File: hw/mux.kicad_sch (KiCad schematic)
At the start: 4 parts, among them U11 NCP708, U6 TS3USB3031

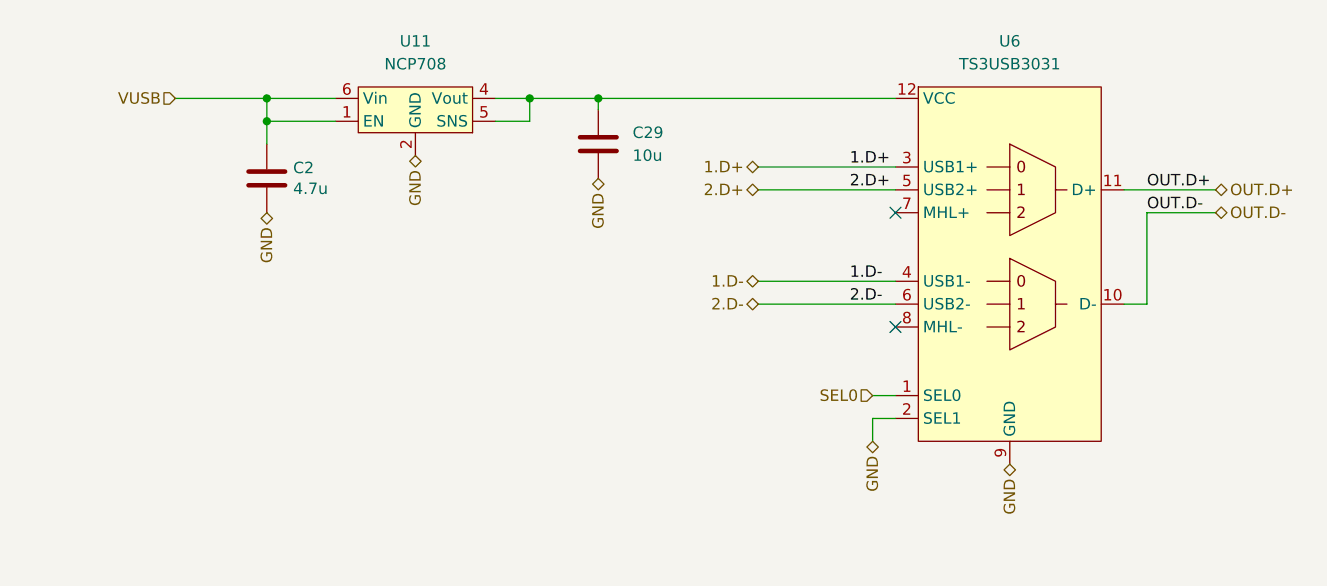
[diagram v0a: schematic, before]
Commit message: Solved issue "Invert INOKB->USB Mux logic"
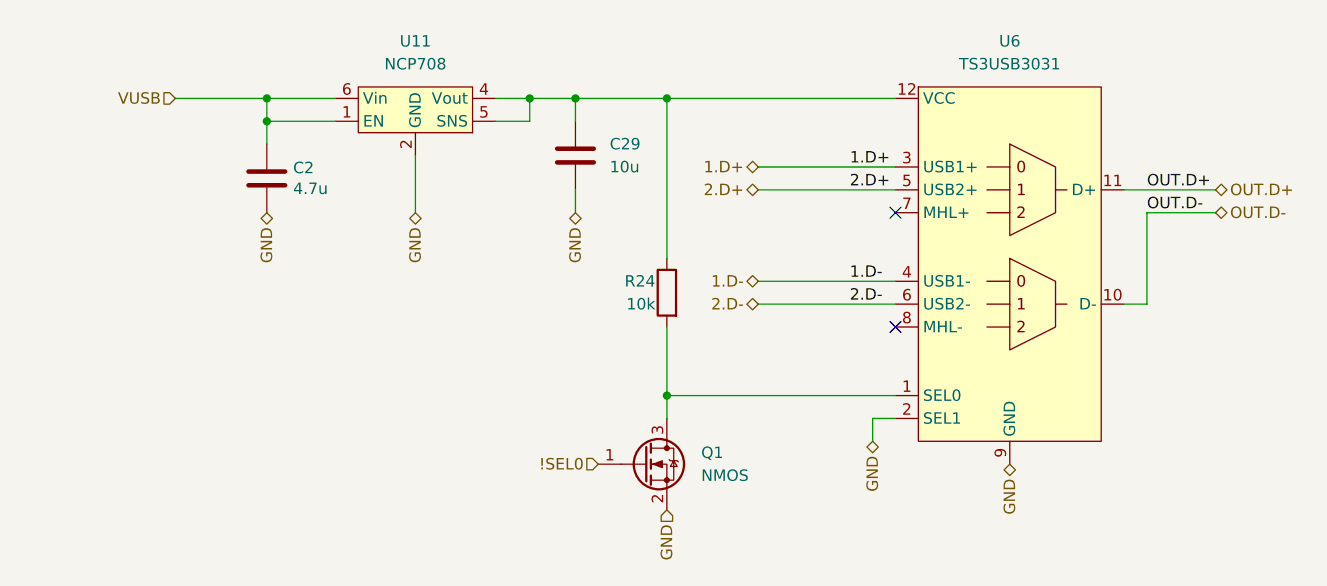
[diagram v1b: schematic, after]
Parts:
- added Q1: NMOS, Package_TO_SOT_SMD:SOT-723, symbol Device:Q_NMOS_GSD
- added R24: 10k, Resistor_SMD:R_0402_1005Metric, symbol Device:R
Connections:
- net GND: now also Q1.2 (S)
- net at C29.1, U11.4 (Vout), U11.5 (SNS)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: now also R24.1
- net SEL0: no longer names the net of U6.1 (SEL0)
- net SEL0: now also Q1.3 (D), R24.2
- new net !SEL0: Q1.1 (G)
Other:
- moved on the sheet: C29
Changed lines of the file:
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@@
   (junction (at 110.49 63.5) (diameter 0) (color 0 0 0 0)
   )
+  (junction (at 144.78 63.5) (diameter 0) (color 0 0 0 0)
+  )
   (junction (at 139.7 63.5) (diameter 0) (color 0 0 0 0)
   )
+  (junction (at 154.94 96.52) (diameter 0) (color 0 0 0 0)
+  )
   (junction (at 110.49 66.04) (diameter 0) (color 0 0 0 0)
   )
-  (junction (at 147.32 63.5) (diameter 0) (color 0 0 0 0)
+  (junction (at 154.94 63.5) (diameter 0) (color 0 0 0 0)
   )
   (no_connect (at 180.34 76.2))
@@
     (stroke (width 0) (type default))
   )
+  (wire (pts (xy 154.94 63.5) (xy 180.34 63.5))
+    (stroke (width 0) (type default))
+  )
   (wire (pts (xy 139.7 66.04) (xy 139.7 63.5))
     (stroke (width 0) (type default))
@@
     (stroke (width 0) (type default))
   )
-  (wire (pts (xy 147.32 63.5) (xy 147.32 64.77))
+  (wire (pts (xy 154.94 88.9) (xy 154.94 96.52))
+    (stroke (width 0) (type default))
+  )
+  (wire (pts (xy 144.78 63.5) (xy 144.78 66.04))
     (stroke (width 0) (type default))
   )
@@
     (stroke (width 0) (type default))
   )
-  (wire (pts (xy 139.7 63.5) (xy 147.32 63.5))
+  (wire (pts (xy 139.7 63.5) (xy 144.78 63.5))
+    (stroke (width 0) (type default))
+  )
+  (wire (pts (xy 154.94 99.06) (xy 154.94 96.52))
+    (stroke (width 0) (type default))
+  )
+  (wire (pts (xy 144.78 63.5) (xy 154.94 63.5))
+    (stroke (width 0) (type default))
+  )
+  (wire (pts (xy 154.94 63.5) (xy 154.94 81.28))
     (stroke (width 0) (type default))
   )
@@
     (stroke (width 0) (type default))
   )
-  (wire (pts (xy 177.8 96.52) (xy 180.34 96.52))
+  (wire (pts (xy 127 76.2) (xy 127 69.85))
     (stroke (width 0) (type default))
   )
@@
     (stroke (width 0) (type default))
   )
+  (wire (pts (xy 154.94 96.52) (xy 180.34 96.52))
+    (stroke (width 0) (type default))
+  )
   (wire (pts (xy 208.28 86.36) (xy 208.28 76.2))
     (stroke (width 0) (type default))
   )
-  (wire (pts (xy 147.32 63.5) (xy 180.34 63.5))
-    (stroke (width 0) (type default))
-  )
   (wire (pts (xy 165.1 71.12) (xy 180.34 71.12))
     (stroke (width 0) (type default))
   )
+  (wire (pts (xy 144.78 76.2) (xy 144.78 73.66))
+    (stroke (width 0) (type default))
+  )
   (wire (pts (xy 110.49 63.5) (xy 100.33 63.5))
     (stroke (width 0) (type default))
@@
     (effects (font (size 1.27 1.27)) (justify right))
   )
-  (hierarchical_label "GND" (shape bidirectional) (at 147.32 72.39 270) (fields_autoplaced)
+  (hierarchical_label "GND" (shape bidirectional) (at 144.78 76.2 270) (fields_autoplaced)
     (effects (font (size 1.27 1.27)) (justify right))
   )
@@
     (effects (font (size 1.27 1.27)) (justify right))
   )
-  (hierarchical_label "GND" (shape bidirectional) (at 127 69.85 270) (fields_autoplaced)
+  (hierarchical_label "GND" (shape bidirectional) (at 127 76.2 270) (fields_autoplaced)
     (effects (font (size 1.27 1.27)) (justify right))
   )
@@
   )
   (hierarchical_label "GND" (shape bidirectional) (at 193.04 104.14 270) (fields_autoplaced)
+    (effects (font (size 1.27 1.27)) (justify right))
+  )
+  (hierarchical_label "GND" (shape input) (at 154.94 109.22 270) (fields_autoplaced)
     (effects (font (size 1.27 1.27)) (justify right))
   )
@@
     (effects (font (size 1.27 1.27)) (justify right))
   )
-  (hierarchical_label "SEL0" (shape input) (at 177.8 96.52 180) (fields_autoplaced)
+  (hierarchical_label "!SEL0" (shape input) (at 147.32 104.14 180) (fields_autoplaced)
     (effects (font (size 1.27 1.27)) (justify right))
   )
   (hierarchical_label "OUT.D-" (shape bidirectional) (at 215.9 76.2 0) (fields_autoplaced)
     (effects (font (size 1.27 1.27)) (justify left))
+  )
+  (symbol (lib_id "Device:Q_NMOS_GSD") (at 152.4 104.14 0) (unit 1)
+    (in_bom yes) (on_board yes) (dnp no)
+    (property "Reference" "Q1" (at 158.75 102.87 0)
+      (effects (font (size 1.27 1.27)) (justify left))
+    )
+    (property "Value" "NMOS" (at 158.75 105.41 0)
+      (effects (font (size 1.27 1.27)) (justify left))
+    )
+    (property "Footprint" "Package_TO_SOT_SMD:SOT-723" (at 157.48 101.6 0)
+      (effects (font (size 1.27 1.27)) hide)
+    )
+    (property "Datasheet" "~" (at 152.4 104.14 0)
+      (effects (font (size 1.27 1.27)) hide)
+    )
+    (property "Sim.Device" "NMOS" (at 152.4 121.285 0)
+      (effects (font (size 1.27 1.27)) hide)
+    )
+    (property "Sim.Type" "VDMOS" (at 152.4 123.19 0)
+      (effects (font (size 1.27 1.27)) hide)
+    )
+    (property "Sim.Pins" "1=D 2=G 3=S" (at 152.4 119.38 0)
+      (effects (font (size 1.27 1.27)) hide)
+    )
+    (property "LCSC" "C504051" (at 152.4 104.14 0)
+      (effects (font (size 1.27 1.27)) hide)
+    )
+    (property "Basic/Extended" "E" (at 152.4 104.14 0)
+      (effects (font (size 1.27 1.27)) hide)
+    )
+    (property "JLCPCB_CORRECTION" "0;0;180" (at 152.4 104.14 0)
+      (effects (font (size 1.27 1.27)) hide)
+    )
+    (pin "1")
+    (pin "2")
+    (pin "3")
+    (instances
+      (project "Zelvicka"
+        (path "/04d53a73-373f-40ca-9ff1-406e2f105d42/b25751f2-11c3-433a-b099-5c0b39b7078e"
+          (reference "Q1") (unit 1)
+        )
+        (path "/04d53a73-373f-40ca-9ff1-406e2f105d42"
+          (reference "Q2") (unit 1)
+        )
+        (path "/04d53a73-373f-40ca-9ff1-406e2f105d42/cf5a8cac-e720-4f6c-b6d8-8f40c3604d15/5f9eb313-4daf-4894-964c-3ee2f806bea1"
+          (reference "Q2") (unit 1)
+        )
+      )
+    )
   )
   (symbol (lib_id "Device:C") (at 110.49 72.39 0) (unit 1)
@@
         (path "/dc7f8a41-3453-4df6-94dc-e94521e89591/9c917b4f-c6c7-4191-9aaa-f982c264da50/8773969d-b2cc-42c4-9a6d-35c6f165cf16/da5be375-027b-4f55-96f0-042c23671c4c"
           (reference "U?") (unit 1)
+        )
+      )
+    )
+  )
+  (symbol (lib_id "Device:R") (at 154.94 85.09 0) (mirror y) (unit 1)
+    (in_bom yes) (on_board yes) (dnp no)
+    (property "Reference" "R24" (at 153.67 83.82 0)
+      (effects (font (size 1.27 1.27)) (justify left))
+    )
+    (property "Value" "10k" (at 153.67 86.36 0)
+      (effects (font (size 1.27 1.27)) (justify left))
+    )
+    (property "Footprint" "Resistor_SMD:R_0402_1005Metric" (at 156.718 85.09 90)
+      (effects (font (size 1.27 1.27)) hide)
+    )
+    (property "Datasheet" "~" (at 154.94 85.09 0)
+      (effects (font (size 1.27 1.27)) hide)
+    )
+    (property "LCSC" "C25744" (at 154.94 85.09 0)
+      (effects (font (size 1.27 1.27)) hide)
+    )
+    (property "JLCPCB_CORRECTION" "" (at 154.94 85.09 0)
+      (effects (font (size 1.27 1.27)) hide)
+    )
+    (property "Basic/Extended" "B" (at 154.94 85.09 0)
+      (effects (font (size 1.27 1.27)) hide)
+    )
+    (pin "1")
+    (pin "2")
+    (instances
+      (project "Zelvicka"
+        (path "/04d53a73-373f-40ca-9ff1-406e2f105d42/75e5fa41-7632-4cae-90f1-8adc7193968e"
+          (reference "R24") (unit 1)
+        )
+        (path "/04d53a73-373f-40ca-9ff1-406e2f105d42"
+          (reference "R53") (unit 1)
+        )
+        (path "/04d53a73-373f-40ca-9ff1-406e2f105d42/cf5a8cac-e720-4f6c-b6d8-8f40c3604d15/5f9eb313-4daf-4894-964c-3ee2f806bea1"
+          (reference "R53") (unit 1)
+        )
+      )
+      (project "ZakladniElektronika"
+        (path "/99cd3e15-4eb6-4cbb-8726-789aedd3df15/c3b70d9b-0dcb-4344-9507-13ff5b4c000e/3abb0ef0-3dd5-4818-a187-7e9bc43bafd4"
+          (reference "R10") (unit 1)
+        )
+      )
+      (project "ukazka"
+        (path "/cd12e26e-b629-4b29-97b6-fad2d22586bd/36757572-51eb-4462-89f8-08695b992ab6"
+          (reference "R5") (unit 1)
+        )
+      )
+      (project "RB3203"
+        (path "/dc7f8a41-3453-4df6-94dc-e94521e89591/9c917b4f-c6c7-4191-9aaa-f982c264da50/e24a5136-2be4-44de-8181-85cee94a1626"
+          (reference "R?") (unit 1)
         )
       )
@@
     )
   )
-  (symbol (lib_id "Device:C") (at 147.32 68.58 0) (unit 1)
+  (symbol (lib_id "Device:C") (at 144.78 69.85 0) (unit 1)
     (in_bom yes) (on_board yes) (dnp no) (fields_autoplaced)
-    (property "Reference" "C29" (at 151.13 67.3099 0)
-      (effects (font (size 1.27 1.27)) (justify left))
-    )
-    (property "Value" "10u" (at 151.13 69.8499 0)
-      (effects (font (size 1.27 1.27)) (justify left))
-    )
-    (property "Footprint" "Capacitor_SMD:C_0603_1608Metric" (at 148.2852 72.39 0)
-      (effects (font (size 1.27 1.27)) hide)
-    )
-    (property "Datasheet" "~" (at 147.32 68.58 0)
-      (effects (font (size 1.27 1.27)) hide)
-    )
-    (property "LCSC" "C96446" (at 147.32 68.58 0)
-      (effects (font (size 1.27 1.27)) hide)
-    )
-    (property "Basic/Extended" "B" (at 147.32 68.58 0)
-      (effects (font (size 1.27 1.27)) hide)
-    )
-    (property "info" "25V, X5R" (at 147.32 68.58 0)
-      (effects (font (size 1.27 1.27)) hide)
-    )
+    (property "Reference" "C29" (at 148.59 68.5799 0)
+      (effects (font (size 1.27 1.27)) (justify left))
+    )
+    (property "Value" "10u" (at 148.59 71.1199 0)
+      (effects (font (size 1.27 1.27)) (justify left))
+    )
+    (property "Footprint" "Capacitor_SMD:C_0603_1608Metric" (at 145.7452 73.66 0)
+      (effects (font (size 1.27 1.27)) hide)
+    )
+    (property "Datasheet" "~" (at 144.78 69.85 0)
+      (effects (font (size 1.27 1.27)) hide)
+    )
+    (property "LCSC" "C96446" (at 144.78 69.85 0)
+      (effects (font (size 1.27 1.27)) hide)
+    )
+    (property "Basic/Extended" "B" (at 144.78 69.85 0)
+      (effects (font (size 1.27 1.27)) hide)
+    )
+    (property "info" "25V, X5R" (at 144.78 69.85 0)
+      (effects (font (size 1.27 1.27)) hide)
+    )

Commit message: a mixture of everything
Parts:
- removed Q1: NMOS, Package_TO_SOT_SMD:SOT-723, symbol Device:Q_NMOS_GSD
- removed R24: 10k, Resistor_SMD:R_0402_1005Metric, symbol Device:R
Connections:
- net 1.D+: now also U6.5 (USB2+); no longer U6.3 (USB1+)
- net 1.D-: now also U6.6 (USB2-); no longer U6.4 (USB1-)
- net 2.D+: now also U6.3 (USB1+); no longer U6.5 (USB2+)
- net 2.D-: now also U6.4 (USB1-); no longer U6.6 (USB2-)
- net SEL0: now reaches U6.1 (SEL0)
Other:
- moved on the sheet: U6

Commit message: wip
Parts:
- added R63: 10k, Resistor_SMD:R_0402_1005Metric, symbol Device:R
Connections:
- net SEL0: now also R63.2
- net at C29.1, U11.4 (Vout), U11.5 (SNS)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: now also R63.1
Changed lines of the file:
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@@
 (kicad_sch (version 20230121) (generator eeschema)
   (paper "A4")
+  (junction (at 154.94 63.5) (diameter 0) (color 0 0 0 0)
+  )
   (junction (at 110.49 63.5) (diameter 0) (color 0 0 0 0)
   )
@@
   )
   (junction (at 110.49 66.04) (diameter 0) (color 0 0 0 0)
+  )
+  (junction (at 154.94 96.52) (diameter 0) (color 0 0 0 0)
   )
   (no_connect (at 167.64 76.2))
@@
     (stroke (width 0) (type default))
   )
+  (wire (pts (xy 154.94 96.52) (xy 167.64 96.52))
+    (stroke (width 0) (type default))
+  )
   (wire (pts (xy 110.49 63.5) (xy 118.11 63.5))
     (stroke (width 0) (type default))
@@
     (stroke (width 0) (type default))
   )
-  (wire (pts (xy 144.78 63.5) (xy 167.64 63.5))
-    (stroke (width 0) (type default))
-  )
-  (wire (pts (xy 165.1 96.52) (xy 167.64 96.52))
+  (wire (pts (xy 154.94 63.5) (xy 154.94 86.36))
+    (stroke (width 0) (type default))
+  )
+  (wire (pts (xy 144.78 63.5) (xy 154.94 63.5))
+    (stroke (width 0) (type default))
+  )
+  (wire (pts (xy 152.4 96.52) (xy 154.94 96.52))
     (stroke (width 0) (type default))
   )
@@
     (stroke (width 0) (type default))
   )
+  (wire (pts (xy 154.94 93.98) (xy 154.94 96.52))
+    (stroke (width 0) (type default))
+  )
   (wire (pts (xy 127 76.2) (xy 127 69.85))
     (stroke (width 0) (type default))
@@
   )
   (wire (pts (xy 110.49 63.5) (xy 100.33 63.5))
+    (stroke (width 0) (type default))
+  )
+  (wire (pts (xy 154.94 63.5) (xy 167.64 63.5))
     (stroke (width 0) (type default))
   )
@@
     (effects (font (size 1.27 1.27)) (justify right))
   )
-  (hierarchical_label "SEL0" (shape input) (at 165.1 96.52 180) (fields_autoplaced)
+  (hierarchical_label "SEL0" (shape input) (at 152.4 96.52 180) (fields_autoplaced)
     (effects (font (size 1.27 1.27)) (justify right))
   )
@@
         )
       )
+    )
+  )
+  (symbol (lib_id "Device:R") (at 154.94 90.17 0) (mirror y) (unit 1)
+    (in_bom yes) (on_board yes) (dnp no)
+    (property "Reference" "R63" (at 152.4 88.9 0)
+      (effects (font (size 1.27 1.27)) (justify left))
+    )
+    (property "Value" "10k" (at 152.4 91.44 0)
+      (effects (font (size 1.27 1.27)) (justify left))
+    )
+    (property "Footprint" "Resistor_SMD:R_0402_1005Metric" (at 156.718 90.17 90)
+      (effects (font (size 1.27 1.27)) hide)
+    )
+    (property "Datasheet" "~" (at 154.94 90.17 0)
+      (effects (font (size 1.27 1.27)) hide)
+    )
+    (property "Basic/Extended" "B" (at 154.94 90.17 0)
+      (effects (font (size 1.27 1.27)) hide)
+    )
+    (property "LCSC" "C25744" (at 154.94 90.17 0)
+      (effects (font (size 1.27 1.27)) hide)
+    )
+    (pin "1")
+    (pin "2")
+    (instances
+      (project "Zelvicka"
+        (path "/04d53a73-373f-40ca-9ff1-406e2f105d42/b25751f2-11c3-433a-b099-5c0b39b7078e/e22ea24c-0368-422d-a8f9-a65d7c1f87fe"
+          (reference "R63") (unit 1)
+        )
+        (path "/04d53a73-373f-40ca-9ff1-406e2f105d42"
+          (reference "R63") (unit 1)
+        )
+        (path "/04d53a73-373f-40ca-9ff1-406e2f105d42/cf5a8cac-e720-4f6c-b6d8-8f40c3604d15/5f9eb313-4daf-4894-964c-3ee2f806bea1"
+          (reference "R63") (unit 1)
+        )
+      )

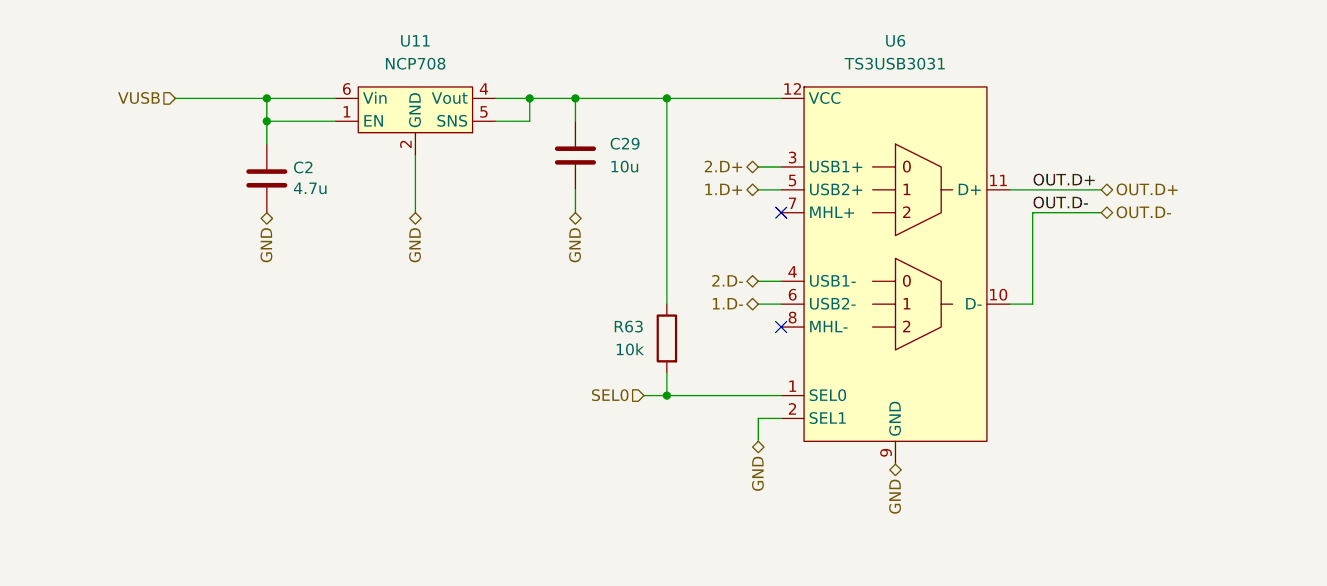
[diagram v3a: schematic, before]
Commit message: Solved issue "Add pull-down resistor to MHL mux channel"
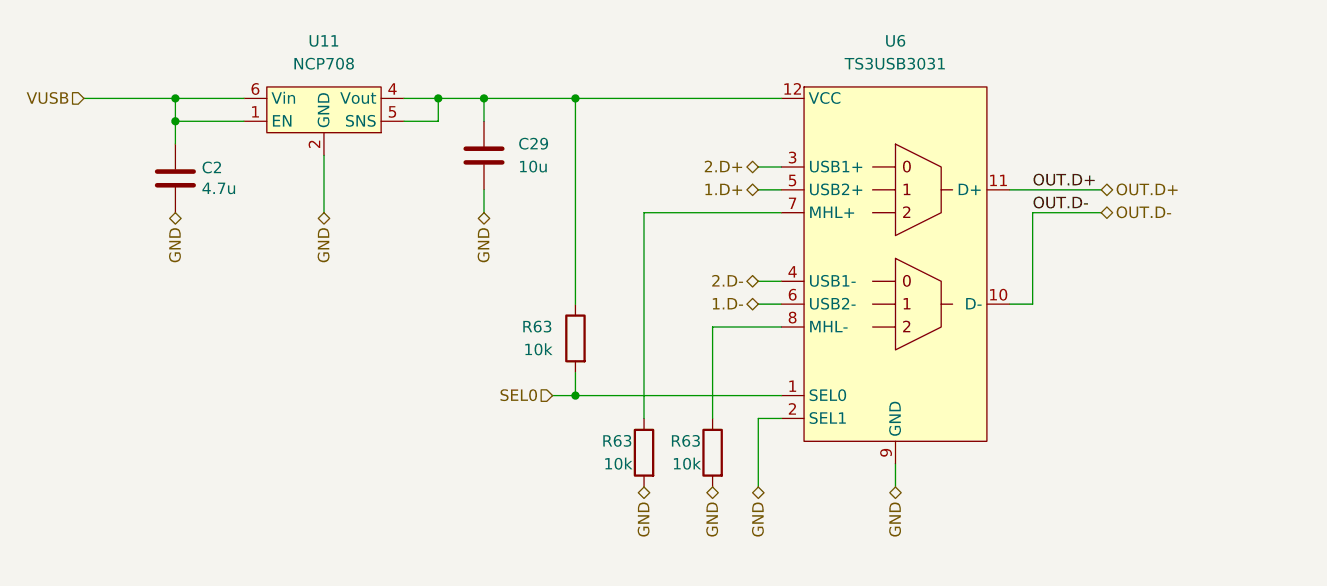
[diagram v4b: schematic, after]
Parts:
- added R63 (x2): 10k, Resistor_SMD:R_0402_1005Metric, symbol Device:R
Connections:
- net GND: now also R63.2, R63.2
- net at U6.7 (MHL+): now also R63.1
- net at U6.8 (MHL-): now also R63.1
- no-connect marks 2 -> 0
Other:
- moved on the sheet: C2, C29, R63, U11
